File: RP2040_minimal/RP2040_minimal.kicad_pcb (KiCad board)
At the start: 4 copper layers, 19.6 x 42.2 mm, 30 parts, among them J1 USB_C_Receptacle_USB2.0, J2 Conn_01x02, J3 Conn_01x16, J4 Conn_01x16, U1 AP2112K-3.3, U2 W25Q128JVS, U3 RP2040, Y1 445C25D12M00000

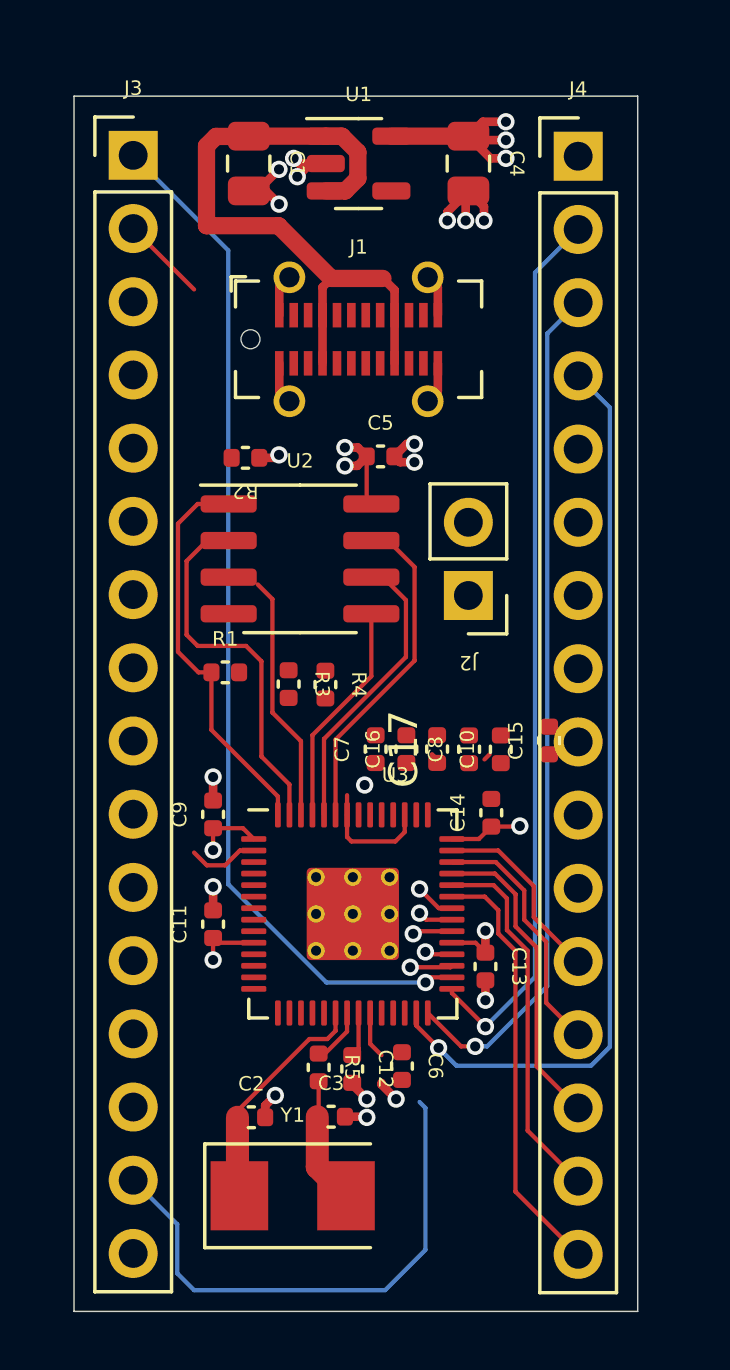
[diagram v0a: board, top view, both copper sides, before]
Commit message: Completed routing
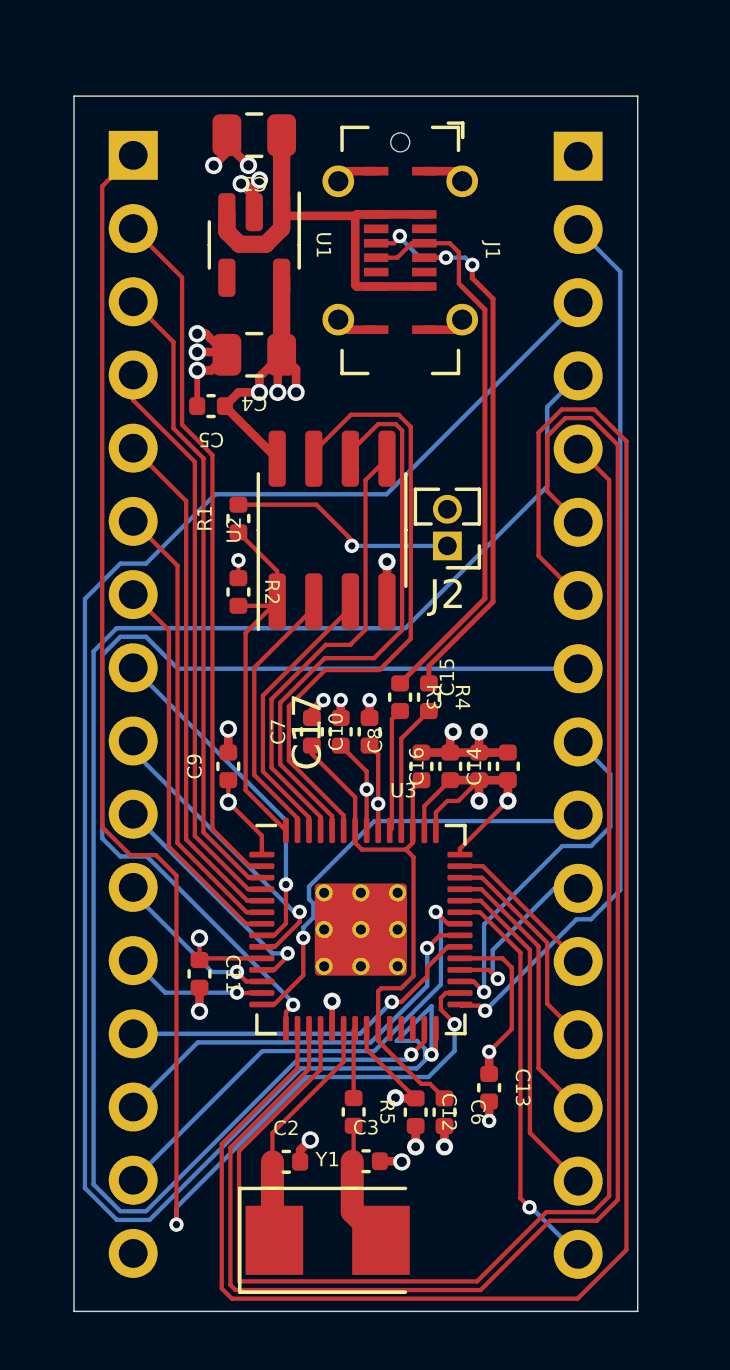
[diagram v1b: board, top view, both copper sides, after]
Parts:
- J2: footprint Connector_PinHeader_2.54mm:PinHeader_1x02_P2.54mm_Vertical -> Connector_PinHeader_1.27mm:PinHeader_1x02_P1.27mm_Vertical
- J3, J4: moved to B.Cu
- moved C4 9.96 mm to (56.0, 51.2), turned to 180 degrees
- moved C5 6.13 mm to (54.5, 53.0), turned to 180 degrees
- moved R1 5.36 mm to (55.4, 56.9), turned to 90 degrees
- moved R2 4.66 mm to (55.4, 59.4), turned to -90 degrees
- moved C10 4.59 mm to (60.0, 64.3)
- moved U1 4.59 mm to (56.0, 47.4), turned to -90 degrees
- moved C13 4.21 mm to (64.1, 76.6)
- moved R3 3.89 mm to (61.1, 63.1)
- moved R4 3.62 mm to (62.1, 63.1)
- moved J1 3.40 mm to (61.1, 47.6), turned to -90 degrees
- moved C17 3.40 mm to (59.0, 64.3)
- moved C12 2.66 mm to (61.6, 77.5)
- moved C15 2.59 mm to (63.8, 65.5)
- moved C7 2.29 mm to (58.0, 64.3)
- moved C6 2.18 mm to (62.6, 77.5)
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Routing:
- net /A9: track 0.00 -> 63.1 mm
- net /A8: track 0.00 -> 57.6 mm
- net /A13: track 0.00 -> 50.4 mm
- net /A11: track 0.00 -> 33.6 mm, vias 0 -> 1
- net /A17: track 29.7 -> 62.2 mm
- net /A14: track 31.7 -> 55.6 mm
- net +3V3: track 22.5 -> 44.6 mm, vias 10 -> 12
- net /A15: track 0.00 -> 22.1 mm
- net /USB_D-: track 0.00 -> 20.3 mm, vias 0 -> 3
- net /A12: track 0.00 -> 20.0 mm
- net /USB_D+: track 0.00 -> 19.8 mm
- net /A16: track 5.45 -> 24.2 mm
- net /A19: track 35.9 -> 54.4 mm, vias 1 -> 2
- net /A7: track 0.00 -> 17.8 mm
- net /A6: track 0.00 -> 15.7 mm
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
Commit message: Switch to 3/5mm vias
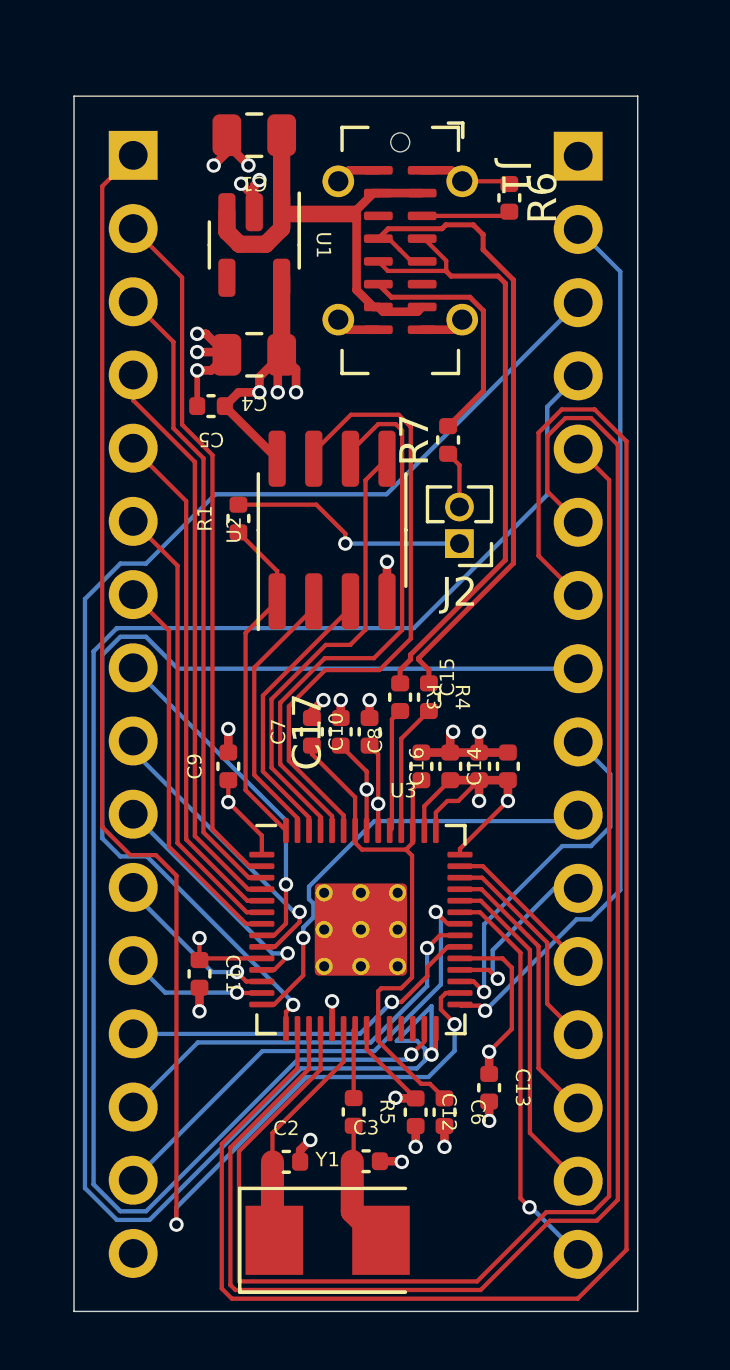
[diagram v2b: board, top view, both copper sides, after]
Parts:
- removed R2: DNF, Capacitor_SMD:C_0402_1005Metric
- added R6: 5.1k, Capacitor_SMD:C_0402_1005Metric, F.Cu at (64.8, 45.7)
- added R7: 5.1k, Capacitor_SMD:C_0402_1005Metric, F.Cu at (62.7, 54.1)
- J1: footprint Connector_USB:USB_C_Receptacle_GCT_USB4115-03-C -> Connector_USB:USB_C_Receptacle_G-Switch_GT-USB-7051x
- U2: value W25Q128JVS -> W25Q16JVSNIQ
- moved J2 0.43 mm to (63.1, 57.7)
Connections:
- J1 pad A5: unconnected-(J1-CC1-PadA5) -> Net-(J1-CC1)
- J1 pad B5: unconnected-(J1-CC2-PadB5) -> Net-(J1-CC2)
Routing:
- net Net-(J1-CC2): track 0.00 -> 8.54 mm
- net GND: track 30.0 -> 34.0 mm
- net VBUS: track 16.1 -> 19.5 mm
- net Net-(J1-CC1): track 0.00 -> 3.09 mm
- net /USB_D-: track 20.3 -> 23.3 mm, vias 3 -> 0
- net /USB_D+: track 19.8 -> 21.6 mm
- net /QSPI_SS: track 13.3 -> 11.9 mm
- net +3V3: track 44.6 -> 44.0 mm, vias 12 -> 11

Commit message: v1.0 submitted for manufacture
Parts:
- moved C13 0.44 mm to (64.6, 76.6)
- moved C9 0.40 mm to (54.7, 65.5)
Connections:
- U3 pad 11: /A2 -> /A8
- U3 pad 12: /A1 -> /A9
- U3 pad 13: /A0 -> /A10
- U3 pad 14: /A10 -> /A11
- U3 pad 15: /A11 -> /A12
- U3 pad 16: /A9 -> /A13
- U3 pad 17: /A8 -> /A14
- U3 pad 18: /A13 -> /A15
- U3 pad 2: /A16 -> /A0
- U3 pad 27: /A14 -> /A16
- U3 pad 3: /A15 -> /A1
- U3 pad 4: /A12 -> /A2
- U3 pad 5: /A7 -> /A3
- U3 pad 6: /A6 -> /A4
- U3 pad 8: /A4 -> /A6
- U3 pad 9: /A3 -> /A7
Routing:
- net /A16: track 24.2 -> 56.8 mm, vias 0 -> 1
- net /A9: track 63.1 -> 37.2 mm, vias 0 -> 1
- net /A8: track 57.6 -> 33.7 mm, vias 0 -> 1
- net /A15: track 22.1 -> 43.6 mm, vias 0 -> 1
- net /A11: track 33.6 -> 18.0 mm
- net /A18: track 30.9 -> 45.6 mm, vias 1 -> 0
- net /A12: track 20.0 -> 28.4 mm
- net /A17: track 62.2 -> 55.0 mm, vias 1 -> 0
- net /A13: track 50.4 -> 54.8 mm, vias 0 -> 1
- net /A7: track 17.8 -> 20.9 mm, vias 0 -> 1
- net /A2: track 8.55 -> 5.58 mm
- net /A0: track 4.93 -> 6.79 mm
- net /~{OE}: track 12.5 -> 10.7 mm, vias 1 -> 2
- net /A6: track 15.7 -> 17.5 mm, vias 0 -> 1
- net /A14: track 55.8 -> 57.4 mm
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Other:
- board text added: "."
- board text added: "A0"
- board text added: "A1"
- board text added: "A10"
- board text added: "A11"
- board text added: "A12"
- board text added: "A13"
- board text added: "A14"
- board text added: "A15"
- board text added: "A16"
- board text added: "A17"
- board text added: "A18"
- board text added: "A19"
- board text added: "A2"
- board text added: "A3"
- board text added: "A4"
- board text added: "A5"
- board text added: "A6"
- board text added: "A7"
- board text added: "A8"
- board text added: "A9"
- board text added: "D0"
- board text added: "D1"
- board text added: "D2"
- board text added: "D3"
- board text added: "D4"
- board text added: "D5"
- board text added: "D6"
- board text added: "D7"
- board text added: "GND"
- board text added: "JLCJLCJLCJLC"
- board text added: "Pico ROM"
- board text added: "v1.0"
- board text added: "~{CE}"
- board text added: "~{OE}"
